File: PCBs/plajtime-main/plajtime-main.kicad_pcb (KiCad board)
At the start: 6 copper layers, 15.2 x 34 mm, 83 parts, among them J1 RP SWD, J2 RP USB, J3 Internal connector, J4 Display connector, J5 Extention connector, J6 Conn_Coaxial, J7 Battery Connector, J8 Nordic SWD, J9 Conn_Coaxial, U1 W25Q64JWU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

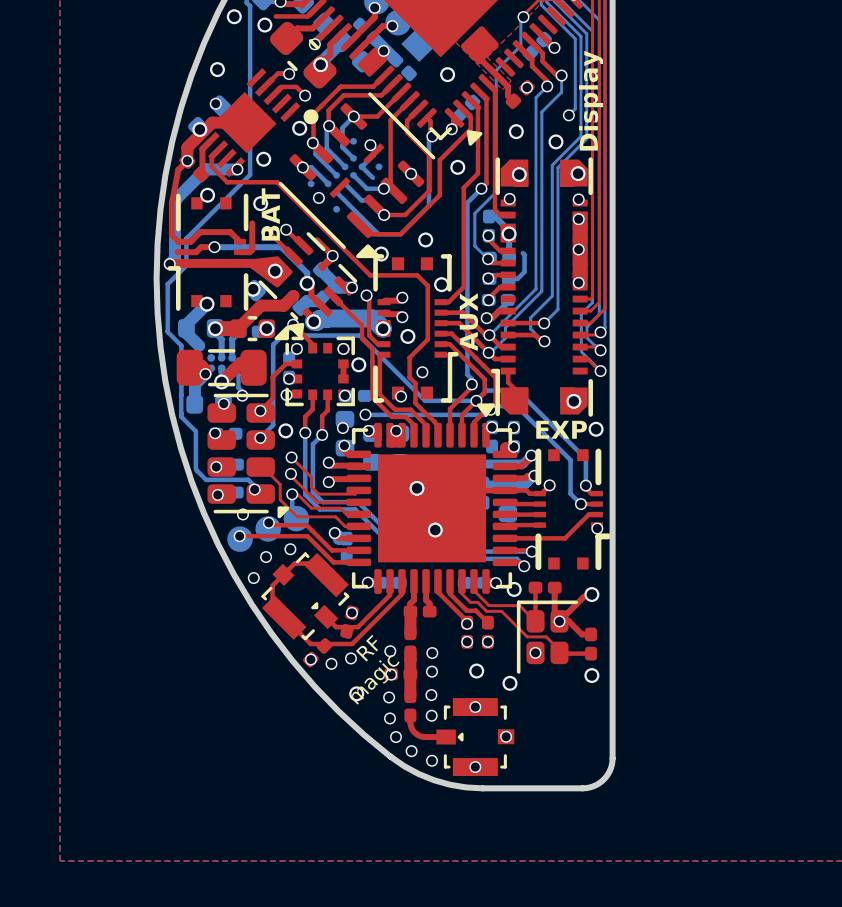
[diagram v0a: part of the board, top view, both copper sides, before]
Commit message: Fixes for bug that I found for now, added right models
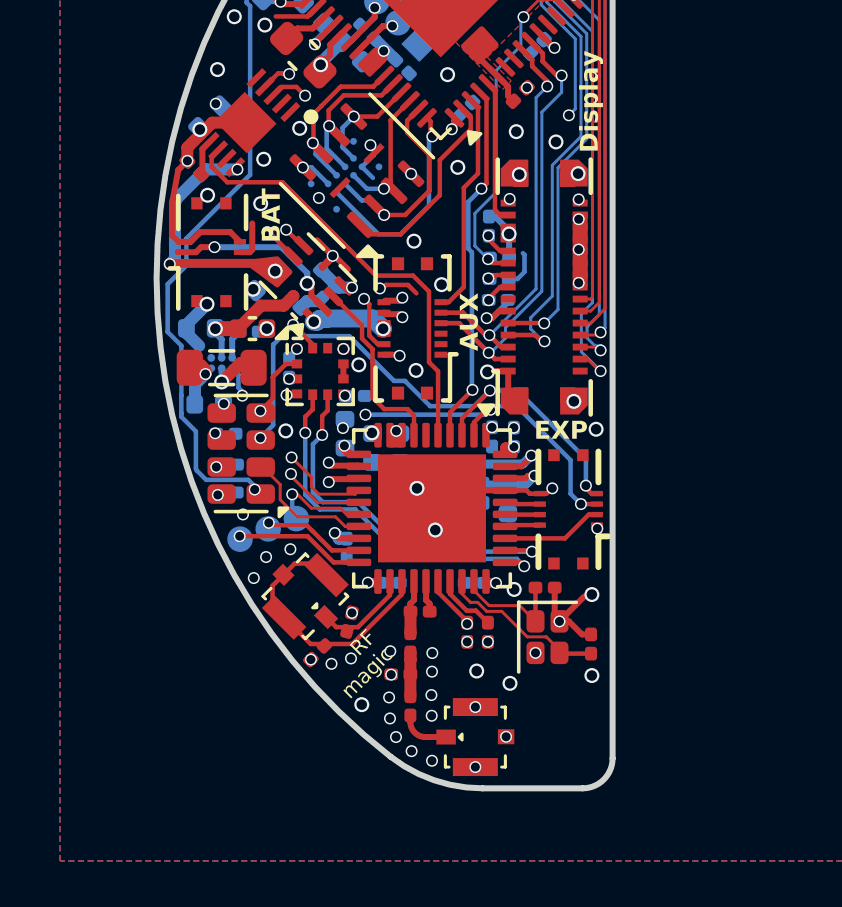
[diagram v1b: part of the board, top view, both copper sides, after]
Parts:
- J8: footprint Library:PinHeader_1x03_P1.00mm_Vertical -> Library:PinHeader_1x03_P1.00mm_Vertical_1
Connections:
- J3 pad 2: SCL -> GND
- J3 pad 3: SDA -> GND
- J3 pad 7: /OXY_INT -> +3V
- U9 pad 6: /OXY_INT -> FREEPIN
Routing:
- net /OXY_INT: track 3.74 -> 0.00 mm
- net SDA: track 34.9 -> 31.2 mm
- net GND: track 22.1 -> 25.2 mm, vias 87 -> 86
- net SCL: track 32.8 -> 30.7 mm
- net /GAUGE_INT: track 15.1 -> 14.5 mm
- net +3V: track 27.0 -> 27.6 mm, vias 25 -> 26

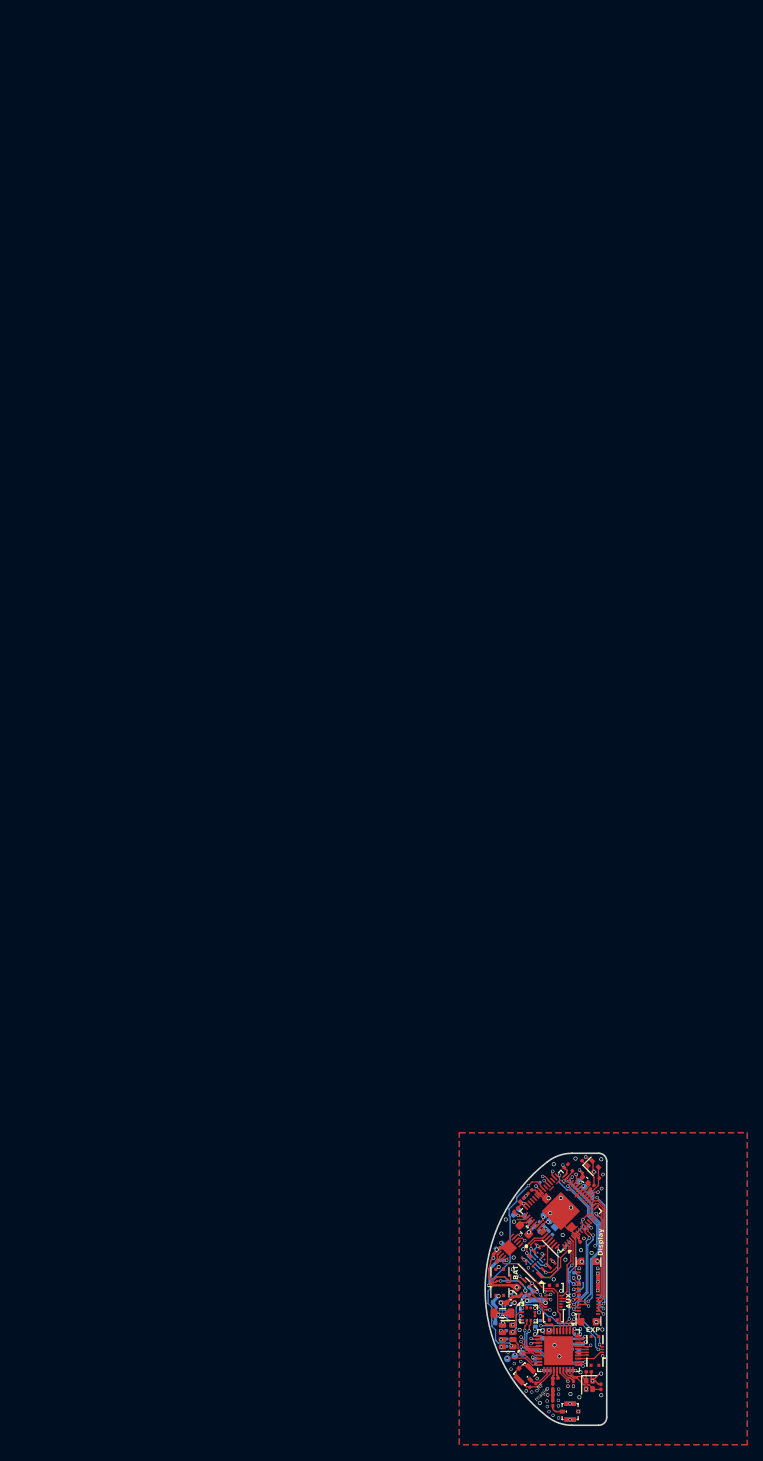
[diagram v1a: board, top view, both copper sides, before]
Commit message: feat: Add new KiCad project for battery flexible PCB, updating main, auxiliary, and 3D models.
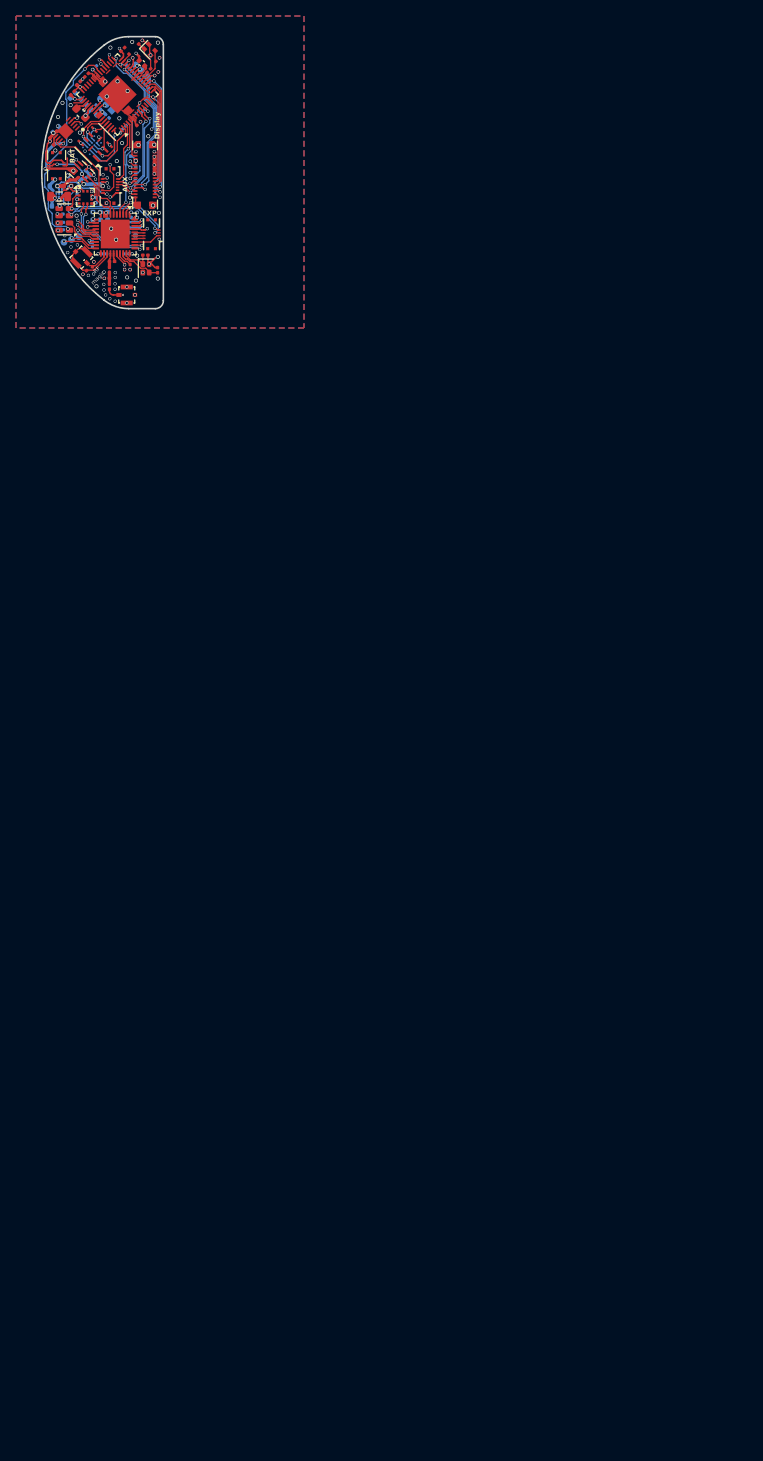
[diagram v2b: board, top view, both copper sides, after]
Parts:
- moved C21 150.6 mm to (-13.4, 3.44), turned to 90 degrees
- moved C41 150.4 mm to (-12.9, 5.41)
- moved C35 150.4 mm to (-12.0, 5.41)
- moved C14 150.2 mm to (-13.2, -8.21)
- moved C16 150.2 mm to (-12.0, -7.06)
- moved C20 150.2 mm to (-13.6, -13.1)
- moved C29 150.2 mm to (-8.29, 5.30)
- moved C30 150.2 mm to (-9.61, 10.2)
- moved C32 150.2 mm to (-5.72, 12.2)
- moved C36 150.2 mm to (-13.9, 9.00)
- moved C37 150.2 mm to (-11.4, 11.1)
- moved C38 150.2 mm to (-9.16, 11.8)
- moved C39 150.2 mm to (-9.02, 5.28)
- moved C4 150.2 mm to (-7.86, -16.3)
- moved C42 150.2 mm to (-9.85, 11.8)
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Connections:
- J3 pad 1: GND -> +3V
- J3 pad 7: +3V -> VSYS
- U9 pad 2: SDA -> SCL
- U9 pad 3: SCL -> SDA
- U9 pad 5: /GAUGE_INT -> FREEPIN
- U9 pad 6: FREEPIN -> /GAUGE_INT
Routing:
- net VSYS: track 7.82 -> 14.8 mm, vias 2 -> 3
- net GND: track 25.2 -> 28.5 mm, vias 86 -> 88
- net SDA: track 31.2 -> 32.9 mm, vias 6 -> 5
- net SCL: track 30.7 -> 29.3 mm
- net /VIC_INT: track 19.3 -> 20.1 mm
- net +3V: track 27.6 -> 28.1 mm
- net +5V: track 6.47 -> 5.94 mm
- net /GAUGE_INT: track 14.5 -> 14.0 mm
